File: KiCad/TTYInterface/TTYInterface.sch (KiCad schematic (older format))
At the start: 9 parts, among them J1 CONN_02X10, J2 DB25_MALE_MountingHoles, U1 MAX3232

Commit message: Update to the PCBs
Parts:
- J1: footprint Connectors_Molex:Molex_Microfit3_Header_02x10_Angled_43045-200x -> Connectors_JST:B20-J11DK_2x10_Pitch2.54mm
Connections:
- net GNDPWR: now also J2.0 (PAD)
- no-connect marks 40 -> 39
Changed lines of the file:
@@
 F 0 "J1" H 3725 5300 50  0000 C CNN
 F 1 "CONN_02X10" V 3725 4750 50  0000 C CNN
-F 2 "Connectors_Molex:Molex_Microfit3_Header_02x10_Angled_43045-200x" H 3725 3550 50  0001 C CNN
+F 2 "Connectors_JST:B20-J11DK_2x10_Pitch2.54mm" H 3725 3550 50  0001 C CNN
 F 3 "" H 3725 3550 50  0001 C CNN
 	1    3725 4750
@@
 Text GLabel 4325 4900 2    60   Input ~ 0
 +5V
-Wire Wire Line
-	5325 3750 4800 3750
-Wire Wire Line
-	5325 4050 4800 4050
-Wire Wire Line
-	6925 3750 7450 3750
-Wire Wire Line
-	6925 4050 7450 4050
-Wire Wire Line
-	6125 3025 6125 3450
-Wire Wire Line
-	6125 6175 6125 5850
-Wire Wire Line
-	5775 5975 6500 5975
-Connection ~ 6125 5975
-Wire Wire Line
-	6925 4250 7125 4250
-Wire Wire Line
-	6925 4550 7125 4550
-Wire Wire Line
-	7425 4250 8375 4250
-Wire Wire Line
-	7675 3275 7675 4550
-Wire Wire Line
-	7425 4550 7900 4550
-Connection ~ 7675 4550
-Connection ~ 7675 4250
-Wire Wire Line
-	5550 3275 7125 3275
-Connection ~ 6125 3275
-Wire Wire Line
-	7425 3275 7675 3275
-Wire Wire Line
-	4325 4500 3975 4500
-Wire Wire Line
-	4325 4900 3975 4900
-Wire Wire Line
-	3975 4800 4150 4800
-Wire Wire Line
-	4150 4800 4150 4500
-Connection ~ 4150 4500
-Wire Wire Line
-	3975 4400 4850 4400
-Wire Wire Line
-	4850 4400 4850 5150
-Wire Wire Line
-	4850 5150 5325 5150
-Wire Wire Line
-	3975 4300 5025 4300
-Wire Wire Line
-	5025 4300 5025 4750
-Wire Wire Line
-	5025 4750 5325 4750
-Wire Wire Line
-	8375 5050 7675 5050
-Wire Wire Line
-	7675 5050 7675 5150
-Wire Wire Line
-	7675 5150 6925 5150
-Wire Wire Line
-	8375 5250 7325 5250
-Wire Wire Line
-	7325 5250 7325 4950
-Wire Wire Line
-	7325 4950 6925 4950
 NoConn ~ 5325 5350
 NoConn ~ 6925 4750
@@
 Text GLabel 7900 5350 2    60   Input ~ 0
 0V
-Wire Wire Line
-	6925 5350 7900 5350
 Text GLabel 5075 4950 0    60   Input ~ 0
 0V
-Wire Wire Line
-	5075 4950 5325 4950
 $Comp
 L R R1
@@
 	1    0    0    -1
 $EndComp
-Wire Wire Line
-	6125 2725 6125 2625
-Wire Wire Line
-	6125 2625 5825 2625
 $Comp
 L DB25_MALE_MountingHoles J2
@@
 	1    0    0    -1
 $EndComp
-NoConn ~ 8675 5650
+Wire Wire Line
+	5325 3750 4800 3750
+Wire Wire Line
+	5325 4050 4800 4050
+Wire Wire Line
+	6925 3750 7450 3750
+Wire Wire Line
+	6925 4050 7450 4050
+Wire Wire Line
+	6125 3025 6125 3450
+Wire Wire Line
+	6125 5850 6125 6175
+Wire Wire Line
+	5775 5975 6500 5975
+Connection ~ 6125 5975
+Wire Wire Line
+	6925 4250 7125 4250
+Wire Wire Line
+	6925 4550 7125 4550
+Wire Wire Line
+	7425 4250 8375 4250
+Wire Wire Line
+	7675 3275 7675 4550
+Wire Wire Line
+	7425 4550 7900 4550
+Connection ~ 7675 4550
+Connection ~ 7675 4250
+Wire Wire Line
+	5550 3275 7125 3275
+Connection ~ 6125 3275
+Wire Wire Line
+	7425 3275 7675 3275
+Wire Wire Line
+	3975 4500 4325 4500
+Wire Wire Line
+	4325 4900 3975 4900
+Wire Wire Line
+	3975 4800 4150 4800
+Wire Wire Line
+	4150 4800 4150 4500
+Connection ~ 4150 4500
+Wire Wire Line
+	3975 4400 4850 4400
+Wire Wire Line
+	4850 4400 4850 5150
+Wire Wire Line
+	4850 5150 5325 5150
+Wire Wire Line
+	3975 4300 5025 4300
+Wire Wire Line
+	5025 4300 5025 4750
+Wire Wire Line
+	5025 4750 5325 4750
+Wire Wire Line
+	8375 5050 7675 5050
+Wire Wire Line
+	7675 5050 7675 5150
+Wire Wire Line
+	7675 5150 6925 5150
+Wire Wire Line
+	8375 5250 7325 5250
+Wire Wire Line
+	7325 5250 7325 4950
+Wire Wire Line
+	7325 4950 6925 4950
+Wire Wire Line
+	6925 5350 7900 5350
+Wire Wire Line
+	5075 4950 5325 4950
+Wire Wire Line
+	6125 2725 6125 2625
+Wire Wire Line
+	6125 2625 5825 2625
+Wire Wire Line
+	6125 5650 6125 5975
+Text GLabel 8675 5925 3    60   Input ~ 0
+0V
+Wire Wire Line
+	8675 5925 8675 5925
+Wire Wire Line
+	8675 5925 8675 5650
 $EndSCHEMATC

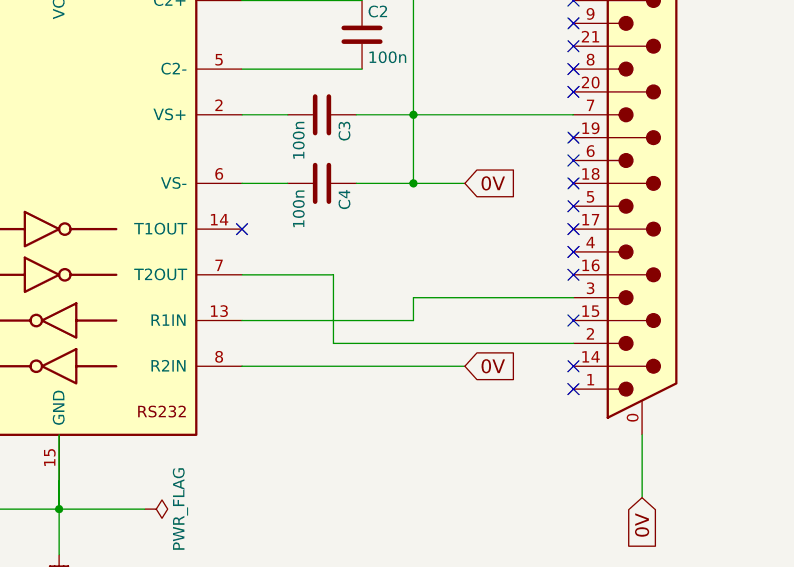
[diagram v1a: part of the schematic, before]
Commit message: Change the TTY circuit
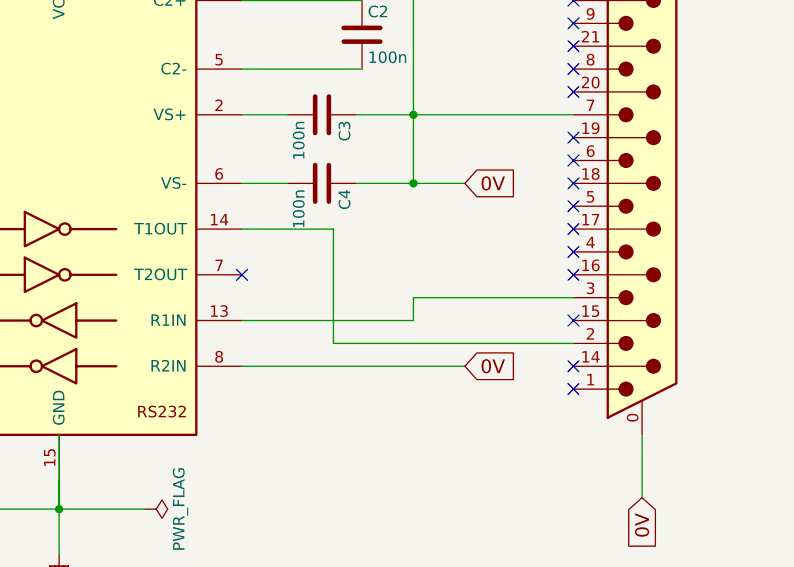
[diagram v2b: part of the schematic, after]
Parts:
- J1: footprint Connectors_JST:B20-J11DK_2x10_Pitch2.54mm -> Pin_Headers:Pin_Header_Angled_2x10_Pitch2.54mm
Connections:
- net at U1.14 (T1OUT): now also J2.2
- net at U1.7 (T2OUT): no longer J2.2
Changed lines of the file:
@@
 F 0 "J1" H 3725 5300 50  0000 C CNN
 F 1 "CONN_02X10" V 3725 4750 50  0000 C CNN
-F 2 "Connectors_JST:B20-J11DK_2x10_Pitch2.54mm" H 3725 3550 50  0001 C CNN
+F 2 "Pin_Headers:Pin_Header_Angled_2x10_Pitch2.54mm" H 3725 3550 50  0001 C CNN
 F 3 "" H 3725 3550 50  0001 C CNN
 	1    3725 4750
@@
 +5V
 NoConn ~ 5325 5350
-NoConn ~ 6925 4750
 NoConn ~ 8375 3050
 NoConn ~ 8375 3150
@@
 	7675 5150 6925 5150
 Wire Wire Line
-	8375 5250 7325 5250
+	7325 5250 8375 5250
 Wire Wire Line
-	7325 5250 7325 4950
-Wire Wire Line
-	7325 4950 6925 4950
+	7325 4750 7325 5250
 Wire Wire Line
 	6925 5350 7900 5350
@@
 Wire Wire Line
 	8675 5925 8675 5650
+NoConn ~ 6925 4950
+Wire Wire Line
+	7325 4750 6925 4750
 $EndSCHEMATC
